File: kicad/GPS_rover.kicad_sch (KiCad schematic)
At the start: 16 parts, among them J401 SMA, U401 ZED_F9R

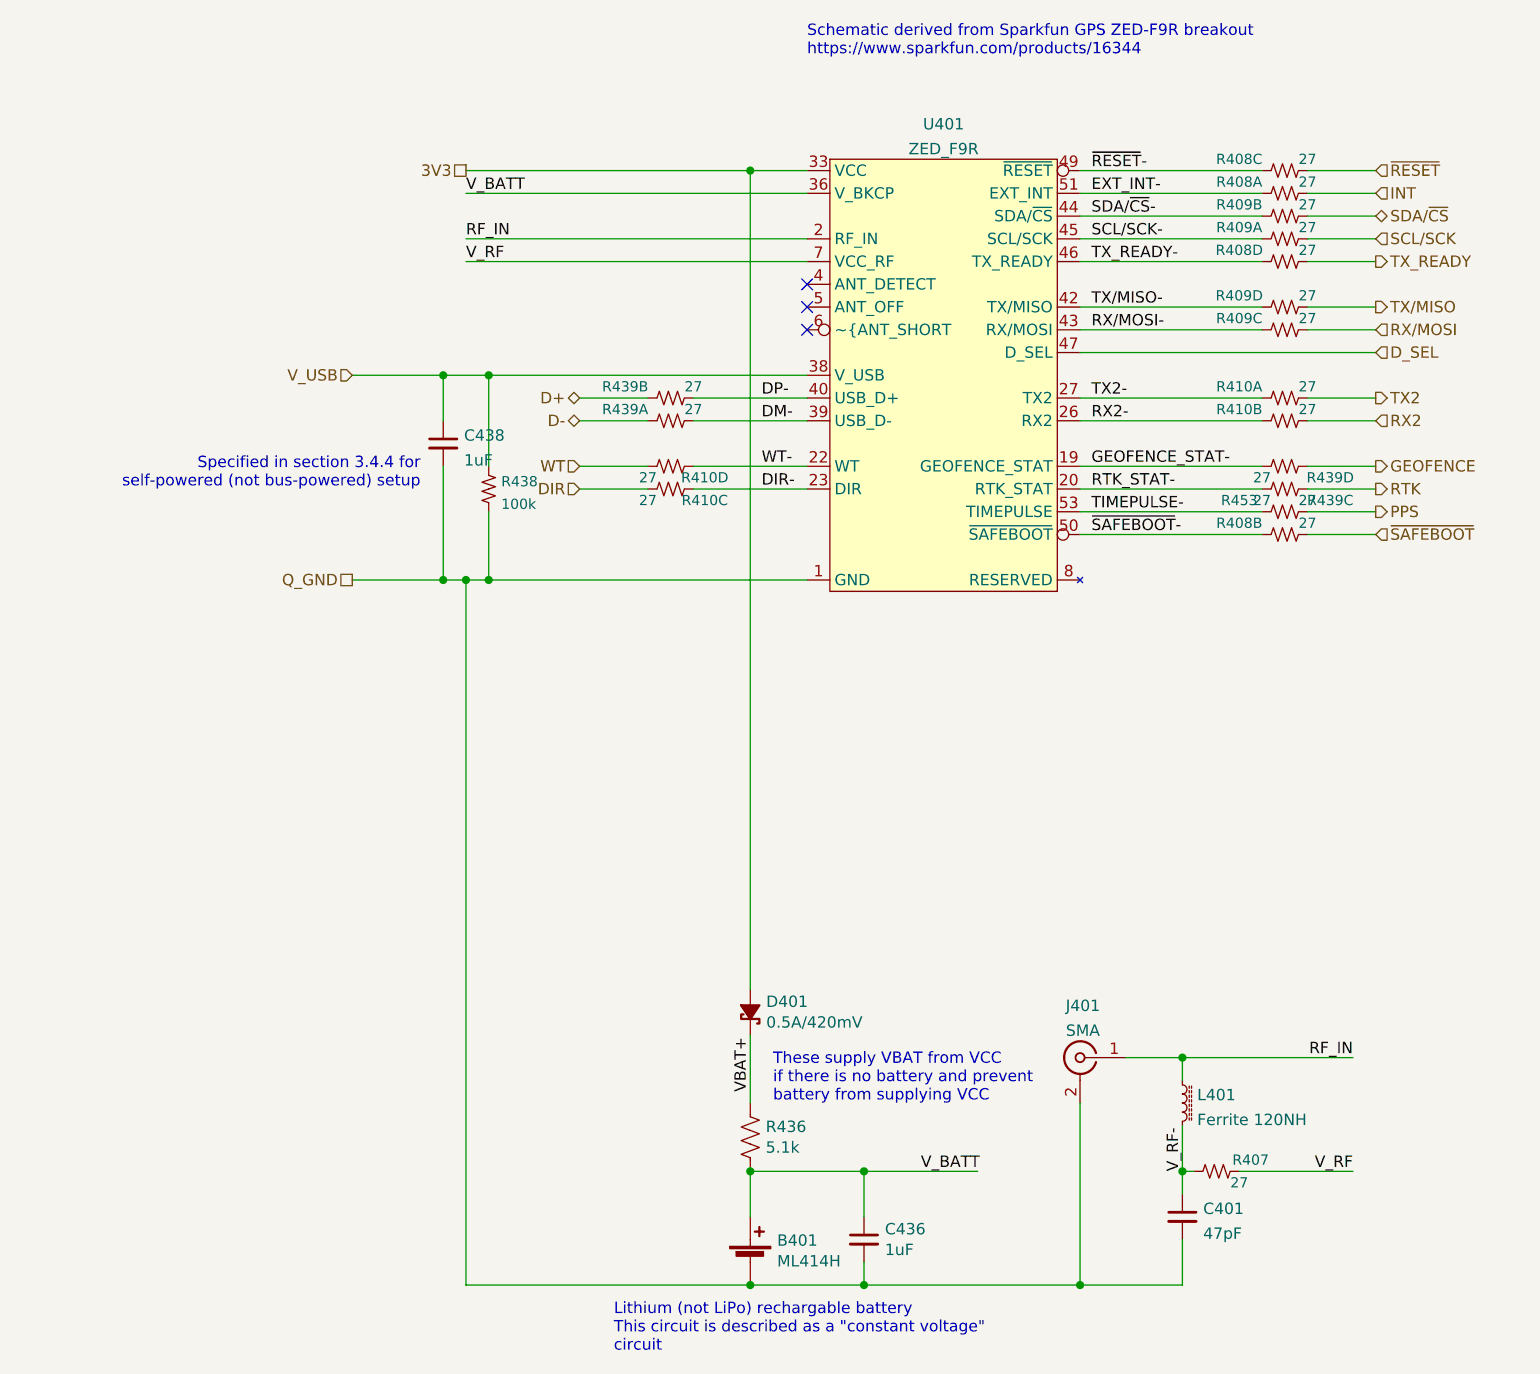
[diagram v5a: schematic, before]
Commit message: Updated antenna chain
Added a BOM-only part to give the actual antenna a Digikey reference that won't appear on the PCB. Added a solder jumper to control whether the antenna is powered. Removed 27R resistors for pins that are not in use.
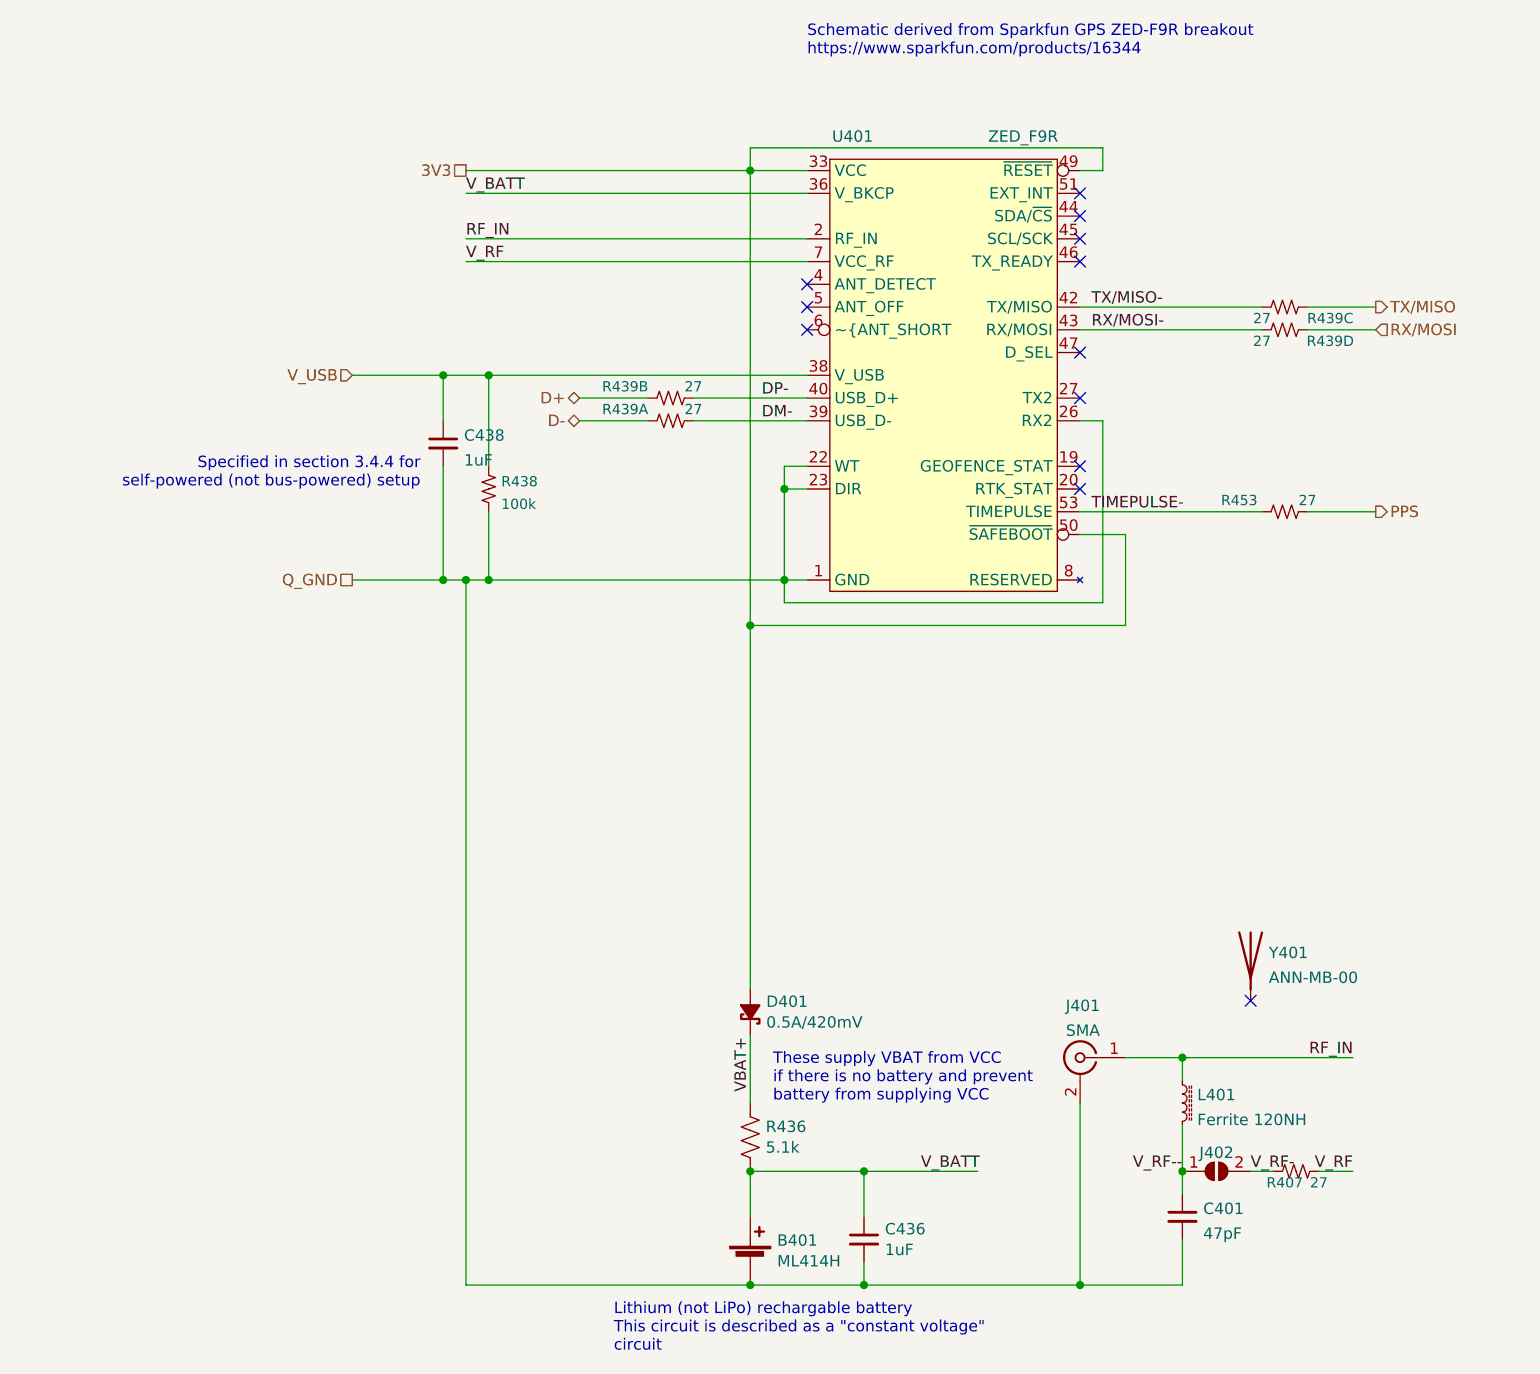
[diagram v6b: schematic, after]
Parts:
- removed R408, R410: 27, KwanSystems:R_Array_Convex_4x0402, symbol KwanSystems:RP4
- removed unit 2 of R409
- removed unit 1 of R409
- removed unit 3 of R439
- removed unit 4 of R439
- added J402: SolderJumper_2_Open, Jumper:SolderJumper-2_P1.3mm_Open_RoundedPad1.0x1.5mm, symbol Jumper:SolderJumper_2_Open
- added Y401: ANN-MB-00, symbol Device:Antenna
- D401: Digikey 641-1520-1-ND -> 641-1332-1-ND
- renumbered R409 to R439
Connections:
- net DIR- is gone; now on net Q_GND: U401.23 (DIR)
- net RX2- is gone; now on net Q_GND: U401.26 (RX2)
- net WT- is gone; now on net Q_GND: U401.22 (WT)
- net ~{RESET}- is gone; now on net 3V3: U401.49 (~{RESET})
- net ~{SAFEBOOT}- is gone; now on net 3V3: U401.50 (~{SAFEBOOT})
- net RX/MOSI: now also R439.4; no longer R439.6 (5)
- net RX/MOSI-: now also R439.5; no longer R439.3 (4)
- net TX/MISO: now also R439.3 (4); no longer R439.5
- net TX/MISO-: now also R439.6 (5); no longer R439.4
- net V_RF-: now also J402.2 (B); no longer C401.1, L401.2
- net D_SEL: no longer names the net of U401.47 (D_SEL)
- net EXT_INT-: no longer names the net of U401.51 (EXT_INT)
- net GEOFENCE_STAT-: no longer names the net of U401.19 (GEOFENCE_STAT)
- net RTK_STAT-: no longer names the net of U401.20 (RTK_STAT)
- net SCL/SCK-: no longer names the net of U401.45 (SCL/SCK)
- net SDA/~{CS}-: no longer names the net of U401.44 (SDA/~{CS})
- net TX2-: no longer names the net of U401.27 (TX2)
- net TX_READY-: no longer names the net of U401.46 (TX_READY)
- new net V_RF--: C401.1, J402.1 (A), L401.2
- no-connect marks 3 -> 12
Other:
- moved on the sheet: R407, R439C, R439D

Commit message: Checkin before branch
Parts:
- J202: renamed from J402; value SolderJumper_2_Open -> NormallyClosed; footprint Jumper:SolderJumper-2_P1.3mm_Open_RoundedPad1.0x1.5mm -> KwanSystems:SolderJumper-2_P1.3mm_MaskBridged_RoundedPad1.0x1.5mm; symbol Jumper:SolderJumper_2_Open -> Jumper:SolderJumper_2_Bridged
- R239: renamed from R439; Digikey 741C083270JPCT-ND -> Y5270CT-ND
- Y401: Purpose (none) -> GPS Antenna
- renumbered B401 to B201, C401 to C201, C436 to C236, C438 to C238, D401 to D201, J401 to J201, L401 to L201, R438 to R238, R453 to R253, U401 to U201
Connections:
- net Q_GND renamed GND
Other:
- company: (none) -> Kwan Systems
- title: (none) -> Rollercoasterometer
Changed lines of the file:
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@@
 (kicad_sch (version 20211123) (generator eeschema)
-  (paper "A4")
+  (paper "USLetter")
+  (title_block
+    (title "Rollercoasterometer")
+    (date "2022-10-07")
+    (company "Kwan Systems")
+  )
   (junction (at 156.21 162.56) (diameter 0) (color 0 0 0 0)
   )
@@
     (effects (font (size 1.27 1.27)) (justify right))
   )
-  (hierarchical_label "Q_GND" (shape passive) (at 63.5 96.52 180)
+  (hierarchical_label "GND" (shape passive) (at 63.5 96.52 180)
     (effects (font (size 1.27 1.27)) (justify right))
   )
@@
   (symbol (lib_id "Device:C_Small") (at 120.65 170.18 0) (unit 1)
     (in_bom yes) (on_board yes)
-    (property "Reference" "C436" (id 0) (at 122.9868 169.0116 0)
+    (property "Reference" "C236" (id 0) (at 122.9868 169.0116 0)
       (effects (font (size 1.27 1.27)) (justify left))
     )
@@
   (symbol (lib_id "KwanSystems:RP4") (at 167.64 66.04 180) (unit 3)
     (in_bom yes) (on_board yes)
-    (property "Reference" "R439" (id 0) (at 172.72 67.31 0)
+    (property "Reference" "R239" (id 0) (at 172.72 67.31 0)
       (effects (font (size 1.143 1.143)))
     )
@@
       (effects (font (size 1.524 1.524)) hide)
     )
-    (property "Digikey" "741C083270JPCT-ND" (id 4) (at 167.64 66.04 0)
+    (property "Digikey" "Y5270CT-ND" (id 4) (at 167.64 66.04 0)
       (effects (font (size 1.27 1.27)) hide)
     )
@@
   (symbol (lib_id "Device:L_Ferrite_Small") (at 156.21 154.94 0) (unit 1)
     (in_bom yes) (on_board yes) (fields_autoplaced)
-    (property "Reference" "L401" (id 0) (at 157.861 154.0315 0)
-      (effects (font (size 1.27 1.27)) (justify left))
-    )
-    (property "Value" "Ferrite 120NH" (id 1) (at 157.861 156.8066 0)
+    (property "Reference" "L201" (id 0) (at 157.861 154.1053 0)
+      (effects (font (size 1.27 1.27)) (justify left))
+    )
+    (property "Value" "Ferrite 120NH" (id 1) (at 157.861 156.6422 0)
       (effects (font (size 1.27 1.27)) (justify left))
     )
@@
   (symbol (lib_id "KwanSystems:RP4") (at 99.06 76.2 0) (unit 2)
     (in_bom yes) (on_board yes)
-    (property "Reference" "R439" (id 0) (at 93.98 74.93 0)
+    (property "Reference" "R239" (id 0) (at 93.98 74.93 0)
       (effects (font (size 1.143 1.143)))
     )
@@
       (effects (font (size 1.524 1.524)) hide)
     )
-    (property "Digikey" "741C083270JPCT-ND" (id 4) (at 99.06 76.2 0)
+    (property "Digikey" "Y5270CT-ND" (id 4) (at 99.06 76.2 0)
       (effects (font (size 1.27 1.27)) hide)
     )
@@
   (symbol (lib_id "Connector:Conn_Coaxial") (at 144.78 149.86 0) (mirror y) (unit 1)
     (in_bom yes) (on_board yes) (fields_autoplaced)
-    (property "Reference" "J401" (id 0) (at 145.0974 144.0669 0))
-    (property "Value" "SMA" (id 1) (at 145.0974 146.842 0))
+    (property "Reference" "J201" (id 0) (at 145.0974 144.3336 0))
+    (property "Value" "SMA" (id 1) (at 145.0974 146.8705 0))
     (property "Footprint" "KwanSystems:SMA-EDGE" (id 2) (at 144.78 149.86 0)
       (effects (font (size 1.27 1.27)) hide)
@@
   (symbol (lib_id "KwanSystems:RP4") (at 99.06 78.74 0) (unit 1)
     (in_bom yes) (on_board yes)
-    (property "Reference" "R439" (id 0) (at 93.98 77.47 0)
+    (property "Reference" "R239" (id 0) (at 93.98 77.47 0)
       (effects (font (size 1.143 1.143)))
     )
@@
       (effects (font (size 1.524 1.524)) hide)
     )
-    (property "Digikey" "741C083270JPCT-ND" (id 4) (at 99.06 78.74 0)
+    (property "Digikey" "Y5270CT-ND" (id 4) (at 99.06 78.74 0)
       (effects (font (size 1.27 1.27)) hide)
     )
@@
   (symbol (lib_id "Device:C_Small") (at 156.21 167.64 0) (unit 1)
     (in_bom yes) (on_board yes) (fields_autoplaced)
-    (property "Reference" "C401" (id 0) (at 158.5341 166.7378 0)
-      (effects (font (size 1.27 1.27)) (justify left))
-    )
-    (property "Value" "47pF" (id 1) (at 158.5341 169.5129 0)
+    (property "Reference" "C201" (id 0) (at 158.5341 166.8116 0)
+      (effects (font (size 1.27 1.27)) (justify left))
+    )
+    (property "Value" "47pF" (id 1) (at 158.5341 169.3485 0)
       (effects (font (size 1.27 1.27)) (justify left))
     )
@@
   (symbol (lib_id "KwanSystems:ZED_F9R") (at 129.54 63.5 0) (unit 1)
     (in_bom yes) (on_board yes)
-    (property "Reference" "U401" (id 0) (at 119.38 46.99 0))
+    (property "Reference" "U201" (id 0) (at 119.38 46.99 0))
     (property "Value" "ZED_F9R" (id 1) (at 138.43 46.99 0))
     (property "Footprint" "KwanSystems:ZED-F9x" (id 2) (at 129.54 63.5 0)
@@
       (effects (font (size 1.27 1.27)) hide)
     )
+    (property "Purpose" "GPS Antenna" (id 5) (at 163.83 138.43 0)
+      (effects (font (size 1.27 1.27)) hide)
+    )
     (pin "1")
   )
@@
     (pin "2")
   )
-  (symbol (lib_id "Jumper:SolderJumper_2_Open") (at 160.02 162.56 0) (unit 1)
+  (symbol (lib_id "Jumper:SolderJumper_2_Bridged") (at 160.02 162.56 0) (unit 1)
     (in_bom no) (on_board yes) (fields_autoplaced)
-    (property "Reference" "J402" (id 0) (at 160.02 160.4795 0))
-    (property "Value" "SolderJumper_2_Open" (id 1) (at 160.02 160.4796 0)
-      (effects (font (size 1.27 1.27)) hide)
-    )
-    (property "Footprint" "Jumper:SolderJumper-2_P1.3mm_Open_RoundedPad1.0x1.5mm" (id 2) (at 160.02 162.56 0)
+    (property "Reference" "J202" (id 0) (at 160.02 160.5082 0))
+    (property "Value" "NormallyClosed" (id 1) (at 160.02 160.4796 0)
+      (effects (font (size 1.27 1.27)) hide)
+    )
+    (property "Footprint" "KwanSystems:SolderJumper-2_P1.3mm_MaskBridged_RoundedPad1.0x1.5mm" (id 2) (at 160.02 162.56 0)
       (effects (font (size 1.27 1.27)) hide)
     )
@@
   (symbol (lib_id "Device:C_Small") (at 73.66 81.28 0) (unit 1)
     (in_bom yes) (on_board yes) (fields_autoplaced)
-    (property "Reference" "C438" (id 0) (at 75.9841 80.3778 0)
-      (effects (font (size 1.27 1.27)) (justify left))
-    )
-    (property "Value" "1uF" (id 1) (at 75.9841 83.1529 0)
+    (property "Reference" "C238" (id 0) (at 75.9841 80.4516 0)
+      (effects (font (size 1.27 1.27)) (justify left))
+    )
+    (property "Value" "1uF" (id 1) (at 75.9841 82.9885 0)
       (effects (font (size 1.27 1.27)) (justify left))
     )
@@
   (symbol (lib_id "KwanSystems:RESISTOR") (at 167.64 88.9 0) (unit 1)
     (in_bom yes) (on_board yes)
-    (property "Reference" "R453" (id 0) (at 162.56 87.63 0)
+    (property "Reference" "R253" (id 0) (at 162.56 87.63 0)
       (effects (font (size 1.143 1.143)))
     )
@@
   (symbol (lib_id "Device:Battery_Cell") (at 107.95 172.72 0) (unit 1)
     (in_bom yes) (on_board yes)
-    (property "Reference" "B401" (id 0) (at 110.9472 170.2816 0)
+    (property "Reference" "B201" (id 0) (at 110.9472 170.2816 0)
       (effects (font (size 1.27 1.27)) (justify left))
     )
@@
   (symbol (lib_id "Device:D_Schottky_Small_Filled") (at 107.95 144.78 270) (mirror x) (unit 1)
     (in_bom yes) (on_board yes)
-    (property "Reference" "D401" (id 0) (at 109.728 143.6116 90)
+    (property "Reference" "D201" (id 0) (at 109.728 143.6116 90)
       (effects (font (size 1.27 1.27)) (justify left))
     )
@@
   (symbol (lib_id "KwanSystems:RP4") (at 167.64 68.58 180) (unit 4)
     (in_bom yes) (on_board yes)
-    (property "Reference" "R439" (id 0) (at 172.72 69.85 0)
+    (property "Reference" "R239" (id 0) (at 172.72 69.85 0)
       (effects (font (size 1.143 1.143)))
     )
@@
       (effects (font (size 1.524 1.524)) hide)
     )
-    (property "Digikey" "741C083270JPCT-ND" (id 4) (at 167.64 68.58 0)
+    (property "Digikey" "Y5270CT-ND" (id 4) (at 167.64 68.58 0)
       (effects (font (size 1.27 1.27)) hide)
     )
@@
   (symbol (lib_id "KwanSystems:RESISTOR") (at 78.74 86.36 90) (unit 1)
     (in_bom yes) (on_board yes) (fields_autoplaced)
-    (property "Reference" "R438" (id 0) (at 80.137 85.5297 90)
+    (property "Reference" "R238" (id 0) (at 80.137 85.5961 90)
       (effects (font (size 1.143 1.143)) (justify right))
     )
-    (property "Value" "100k" (id 1) (at 80.137 88.0525 90)
+    (property "Value" "100k" (id 1) (at 80.137 87.9047 90)
       (effects (font (size 1.143 1.143)) (justify right))
     )
